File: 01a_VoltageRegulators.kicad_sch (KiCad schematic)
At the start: 34 parts, among them U2 TPS54331, U3 TLV75733PDBV, U4 TPS56637RPAR

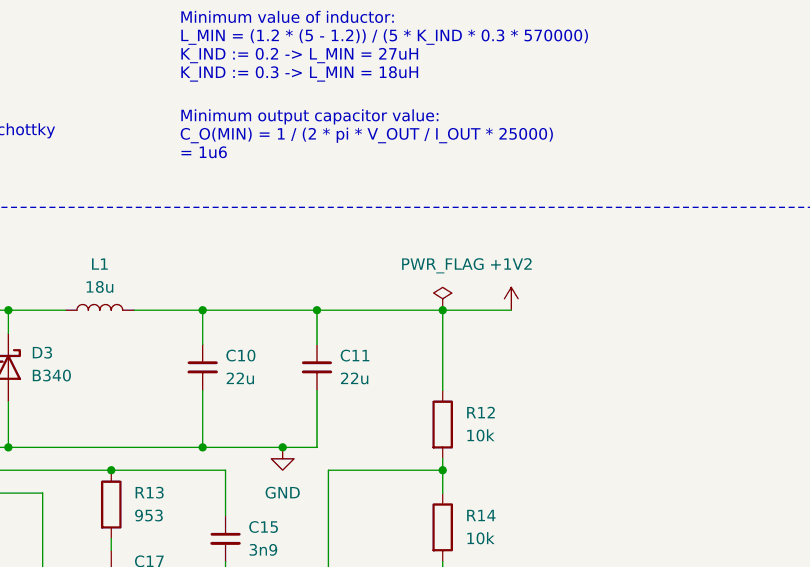
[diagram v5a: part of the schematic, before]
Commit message: symbol fixes, switch ESD protection for USB datalines
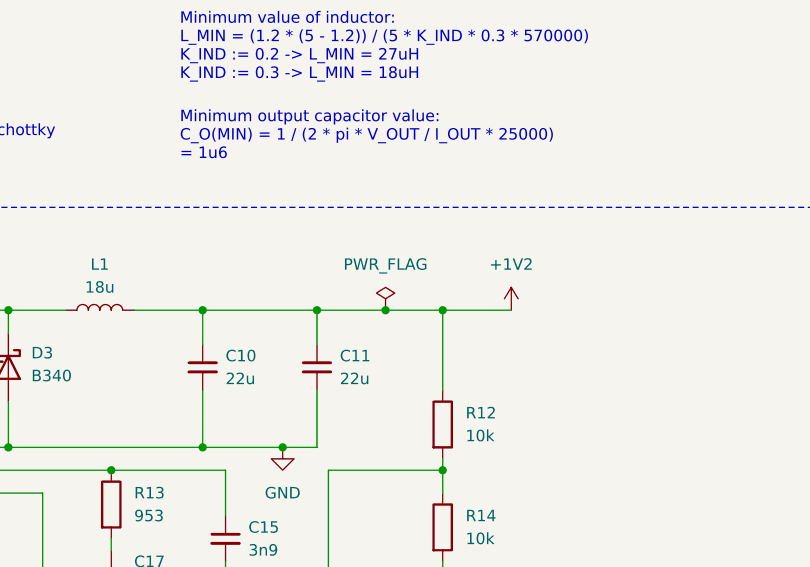
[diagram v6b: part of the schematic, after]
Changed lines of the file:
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@@
   (junction (at 41.91 114.3) (diameter 0) (color 0 0 0 0)
+  )
+  (junction (at 146.05 24.13) (diameter 0) (color 0 0 0 0)
   )
   (junction (at 152.4 24.13) (diameter 0) (color 0 0 0 0)
@@
     (stroke (width 0) (type default))
   )
+  (wire (pts (xy 146.05 24.13) (xy 138.43 24.13))
+    (stroke (width 0) (type default))
+  )
   (wire (pts (xy 107.95 66.04) (xy 139.7 66.04))
     (stroke (width 0) (type default))
@@
     (stroke (width 0) (type default))
   )
-  (wire (pts (xy 152.4 24.13) (xy 138.43 24.13))
-    (stroke (width 0) (type default))
-  )
   (wire (pts (xy 209.55 96.52) (xy 209.55 99.06))
     (stroke (width 0) (type default))
@@
   )
   (wire (pts (xy 147.32 100.33) (xy 157.48 100.33))
+    (stroke (width 0) (type default))
+  )
+  (wire (pts (xy 146.05 24.13) (xy 152.4 24.13))
     (stroke (width 0) (type default))
   )
@@
     )
   )
-  (symbol (lib_id "power:PWR_FLAG") (at 152.4 24.13 0) (unit 1)
-    (in_bom yes) (on_board yes) (dnp no) (fields_autoplaced)
-    (property "Reference" "#FLG01" (at 152.4 22.225 0)
-      (effects (font (size 1.27 1.27)) hide)
-    )
-    (property "Value" "PWR_FLAG" (at 152.4 19.05 0)
-      (effects (font (size 1.27 1.27)))
-    )
-    (property "Footprint" "" (at 152.4 24.13 0)
-      (effects (font (size 1.27 1.27)) hide)
-    )
-    (property "Datasheet" "~" (at 152.4 24.13 0)
-      (effects (font (size 1.27 1.27)) hide)
-    )
+  (symbol (lib_id "power:PWR_FLAG") (at 146.05 24.13 0) (unit 1)
+    (in_bom yes) (on_board yes) (dnp no) (fields_autoplaced)
+    (property "Reference" "#FLG01" (at 146.05 22.225 0)
+      (effects (font (size 1.27 1.27)) hide)
+    )
+    (property "Value" "PWR_FLAG" (at 146.05 19.05 0)
+      (effects (font (size 1.27 1.27)))
+    )
+    (property "Footprint" "" (at 146.05 24.13 0)
+      (effects (font (size 1.27 1.27)) hide)
+    )
+    (property "Datasheet" "~" (at 146.05 24.13 0)
+      (effects (font (size 1.27 1.27)) hide)
+    )

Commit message: fix symbols, route UFP DPs and voltage regs
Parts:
- R12, R14, R15, R17, R18, R20: footprint Resistor_SMD:R_0603_1608Metric -> Resistor_SMD:R_0402_1005Metric
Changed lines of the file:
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@@
       (effects (font (size 1.27 1.27)) (justify left))
     )
-    (property "Footprint" "Resistor_SMD:R_0603_1608Metric" (at 136.652 125.73 90)
+    (property "Footprint" "Resistor_SMD:R_0402_1005Metric" (at 136.652 125.73 90)
       (effects (font (size 1.27 1.27)) hide)
     )
@@
       (effects (font (size 1.27 1.27)))
     )
-    (property "Footprint" "Resistor_SMD:R_0603_1608Metric" (at 134.62 109.728 90)
+    (property "Footprint" "Resistor_SMD:R_0402_1005Metric" (at 134.62 109.728 90)
       (effects (font (size 1.27 1.27)) hide)
     )
@@
       (effects (font (size 1.27 1.27)) (justify left))
     )
-    (property "Footprint" "Resistor_SMD:R_0603_1608Metric" (at 150.622 48.26 90)
+    (property "Footprint" "Resistor_SMD:R_0402_1005Metric" (at 150.622 48.26 90)
       (effects (font (size 1.27 1.27)) hide)
     )
@@
       (effects (font (size 1.27 1.27)))
     )
-    (property "Footprint" "Resistor_SMD:R_0603_1608Metric" (at 127 109.728 90)
+    (property "Footprint" "Resistor_SMD:R_0402_1005Metric" (at 127 109.728 90)
       (effects (font (size 1.27 1.27)) hide)
     )
@@
       (effects (font (size 1.27 1.27)) (justify left))
     )
-    (property "Footprint" "Resistor_SMD:R_0603_1608Metric" (at 150.622 57.15 90)
+    (property "Footprint" "Resistor_SMD:R_0402_1005Metric" (at 150.622 57.15 90)
       (effects (font (size 1.27 1.27)) hide)
     )
@@
       (effects (font (size 1.27 1.27)) (justify left))
     )
-    (property "Footprint" "Resistor_SMD:R_0603_1608Metric" (at 150.622 36.83 90)
-      (effects (font (size 1.27 1.27)) hide)
-    )
+    (property "Footprint" "Resistor_SMD:R_0402_1005Metric" (at 150.622 36.83 90)
+      (effects (font (size 1.27 1.27)) hide)
+    )

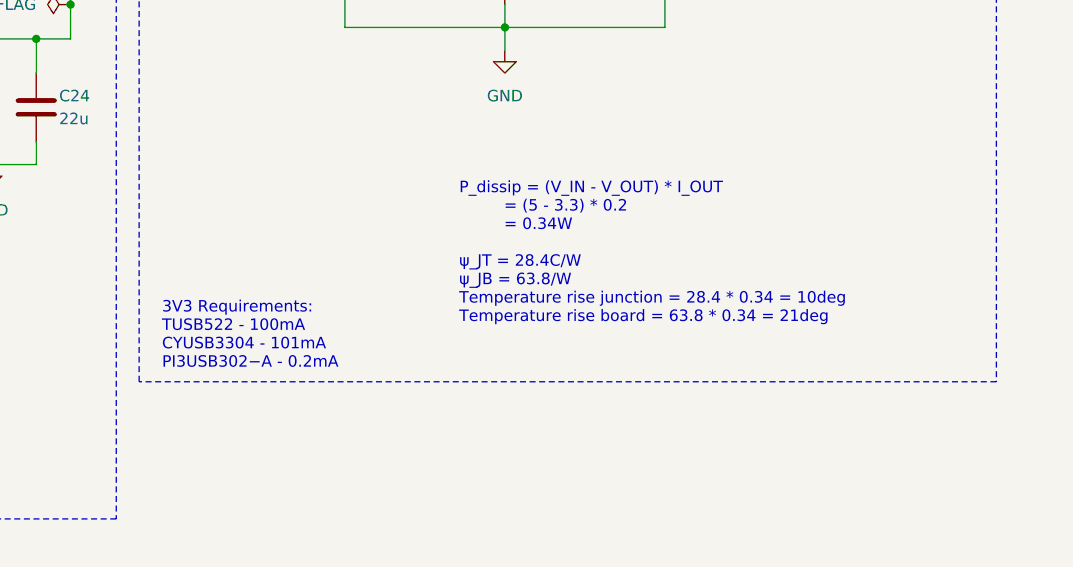
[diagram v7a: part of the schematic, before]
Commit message: add RTL8153
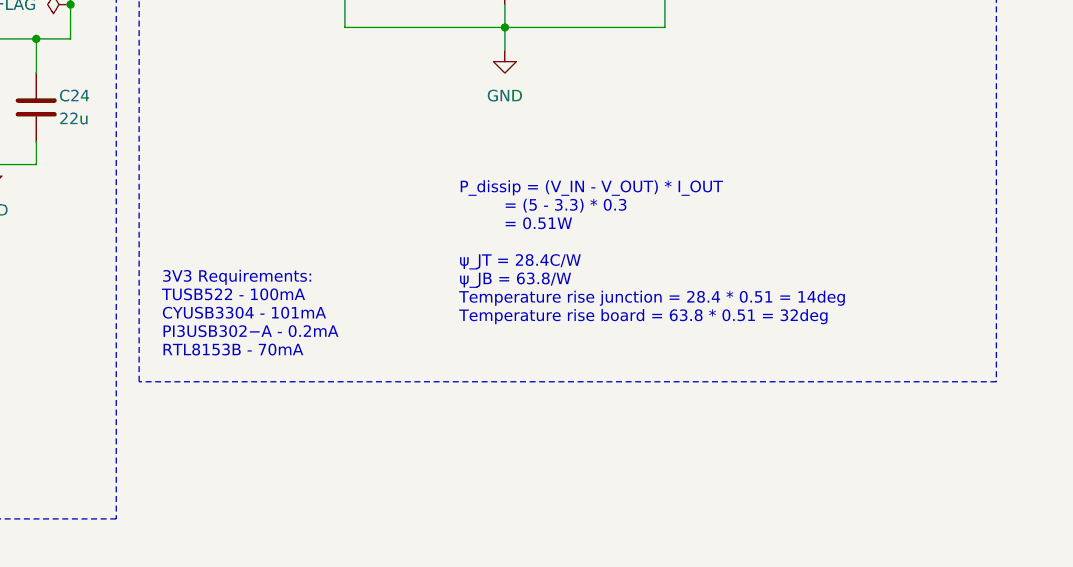
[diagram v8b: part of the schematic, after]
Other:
- note added: "3V3 Requirements: TUSB522 - 100mA CYUSB3304 - 101mA PI3USB302−A - 0.2mA RTL8153B - 70mA"
- note added: "P_dissip = (V_IN - V_OUT) * I_OUT = (5 - 3.3) * 0.3 = 0.51W ψ_JT = 28.4C/W ψ_JB = 63.8/W Temperature rise junction = 28.4 * 0.51 = 14deg Temperature rise board = 63.8 * 0.51 = 32deg"
- note removed: "3V3 Requirements: TUSB522 - 100mA CYUSB3304 - 101mA PI3USB302−A - 0.2mA"
- note removed: "P_dissip = (V_IN - V_OUT) * I_OUT = (5 - 3.3) * 0.2 = 0.34W ψ_JT = 28.4C/W ψ_JB = 63.8/W Temperature rise junction = 28.4 * 0.34 = 10deg Temperature rise board = 63.8 * 0.34 = 21deg"
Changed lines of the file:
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@@
     (effects (font (size 1.27 1.27)) (justify left bottom))
   )
-  (text "3V3 Requirements:\nTUSB522 - 100mA\nCYUSB3304 - 101mA\nPI3USB302−A - 0.2mA"
-    (at 171.45 137.16 0)
+  (text "3V3 Requirements:\nTUSB522 - 100mA\nCYUSB3304 - 101mA\nPI3USB302−A - 0.2mA\nRTL8153B - 70mA"
+    (at 171.45 135.89 0)
     (effects (font (size 1.27 1.27)) (justify left bottom))
   )
@@
     (effects (font (size 1.27 1.27)) (justify left bottom))
   )
-  (text "P_dissip = (V_IN - V_OUT) * I_OUT\n         = (5 - 3.3) * 0.2\n         = 0.34W\n\nψ_JT = 28.4C/W\nψ_JB = 63.8/W\nTemperature rise junction = 28.4 * 0.34 = 10deg\nTemperature rise board = 63.8 * 0.34 = 21deg"
+  (text "P_dissip = (V_IN - V_OUT) * I_OUT\n         = (5 - 3.3) * 0.3\n         = 0.51W\n\nψ_JT = 28.4C/W\nψ_JB = 63.8/W\nTemperature rise junction = 28.4 * 0.51 = 14deg\nTemperature rise board = 63.8 * 0.51 = 32deg"
     (at 204.47 132.08 0)
     (effects (font (size 1.27 1.27)) (justify left bottom))
